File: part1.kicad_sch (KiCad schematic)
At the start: 21 parts, among them U1 74LS377, U10 Am2918, U11 Am2919, U12 Am2919, U13 74LS139, U14 74LS399, U15 74LS175, U16 Am2921, U17 Am2921, U18 Am27S19, U19 Am27S19, U2 Am2919, U3 Am2919, U37 74LS175, U4 Am27S21, U5 Am27S21, U6 Am27S21, U7 Am2910, U8 Am2918, U9 Am2918

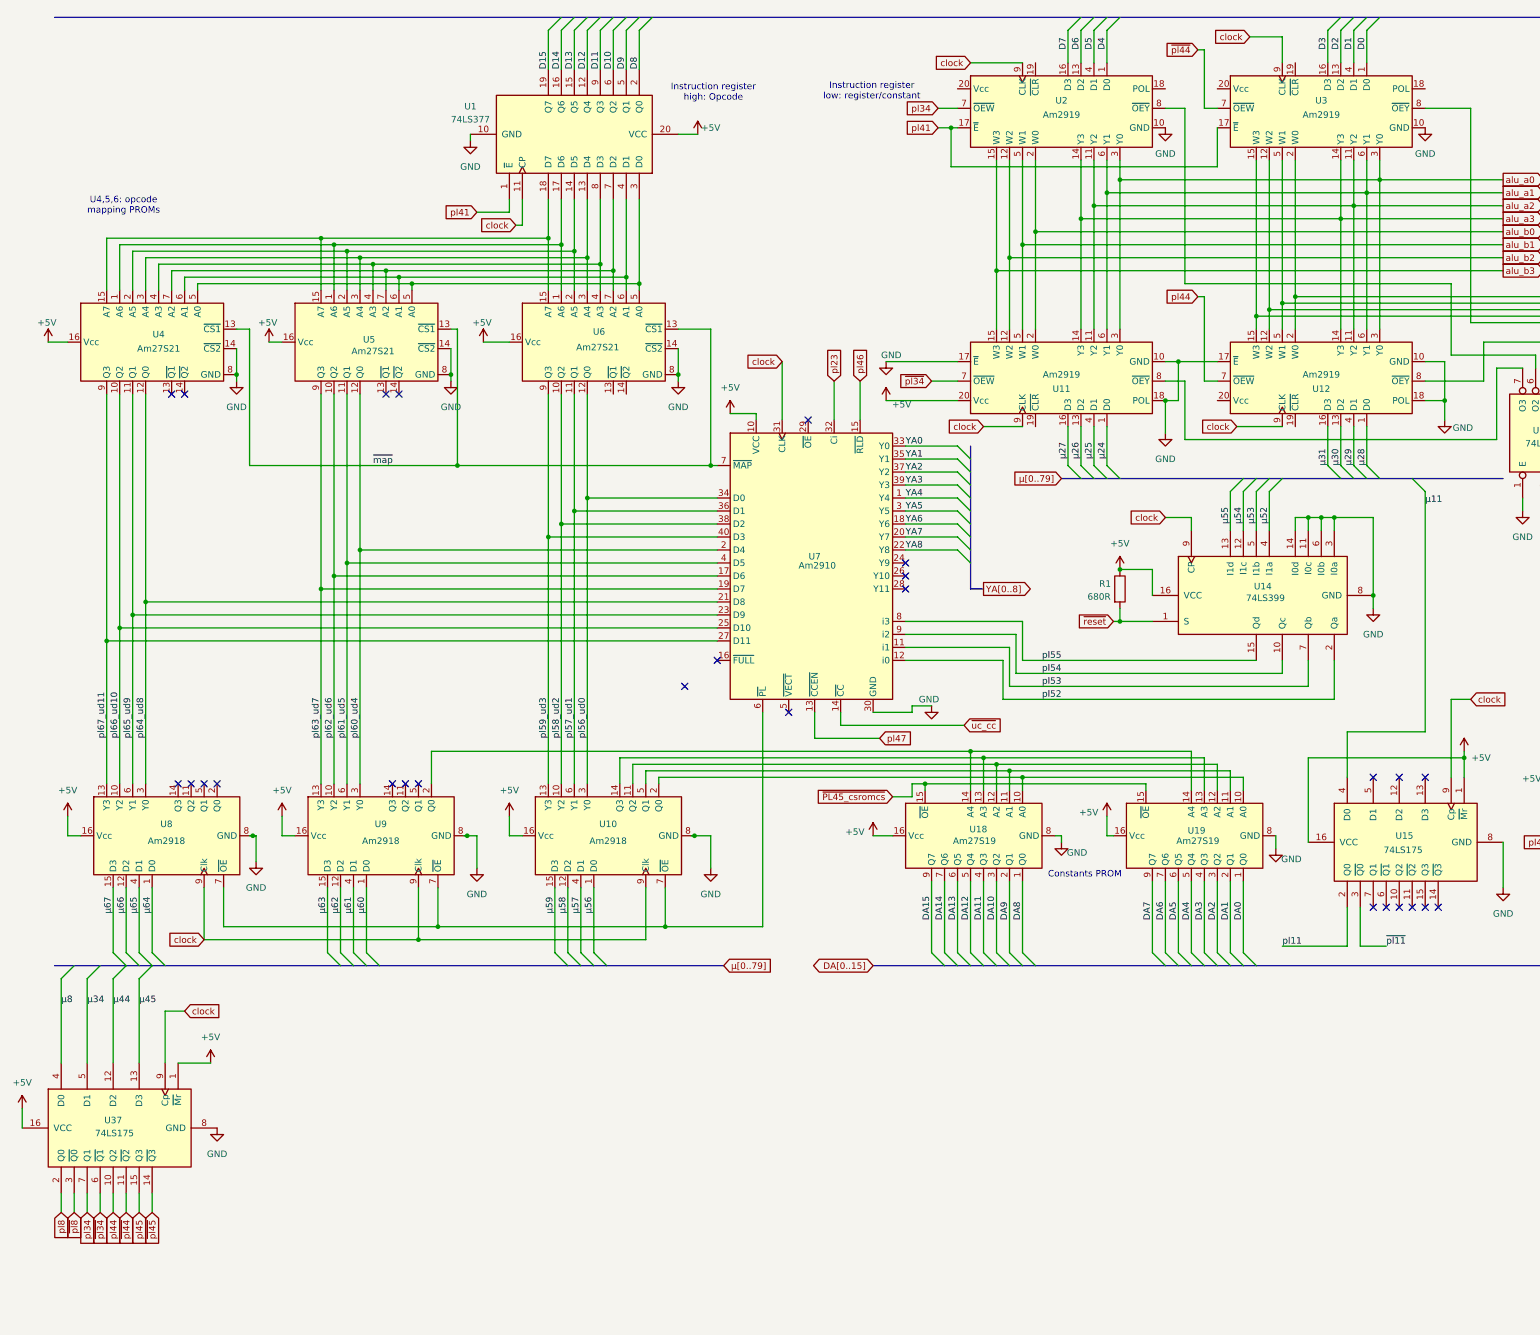
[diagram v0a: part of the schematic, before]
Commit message: Schematic complete wrt original
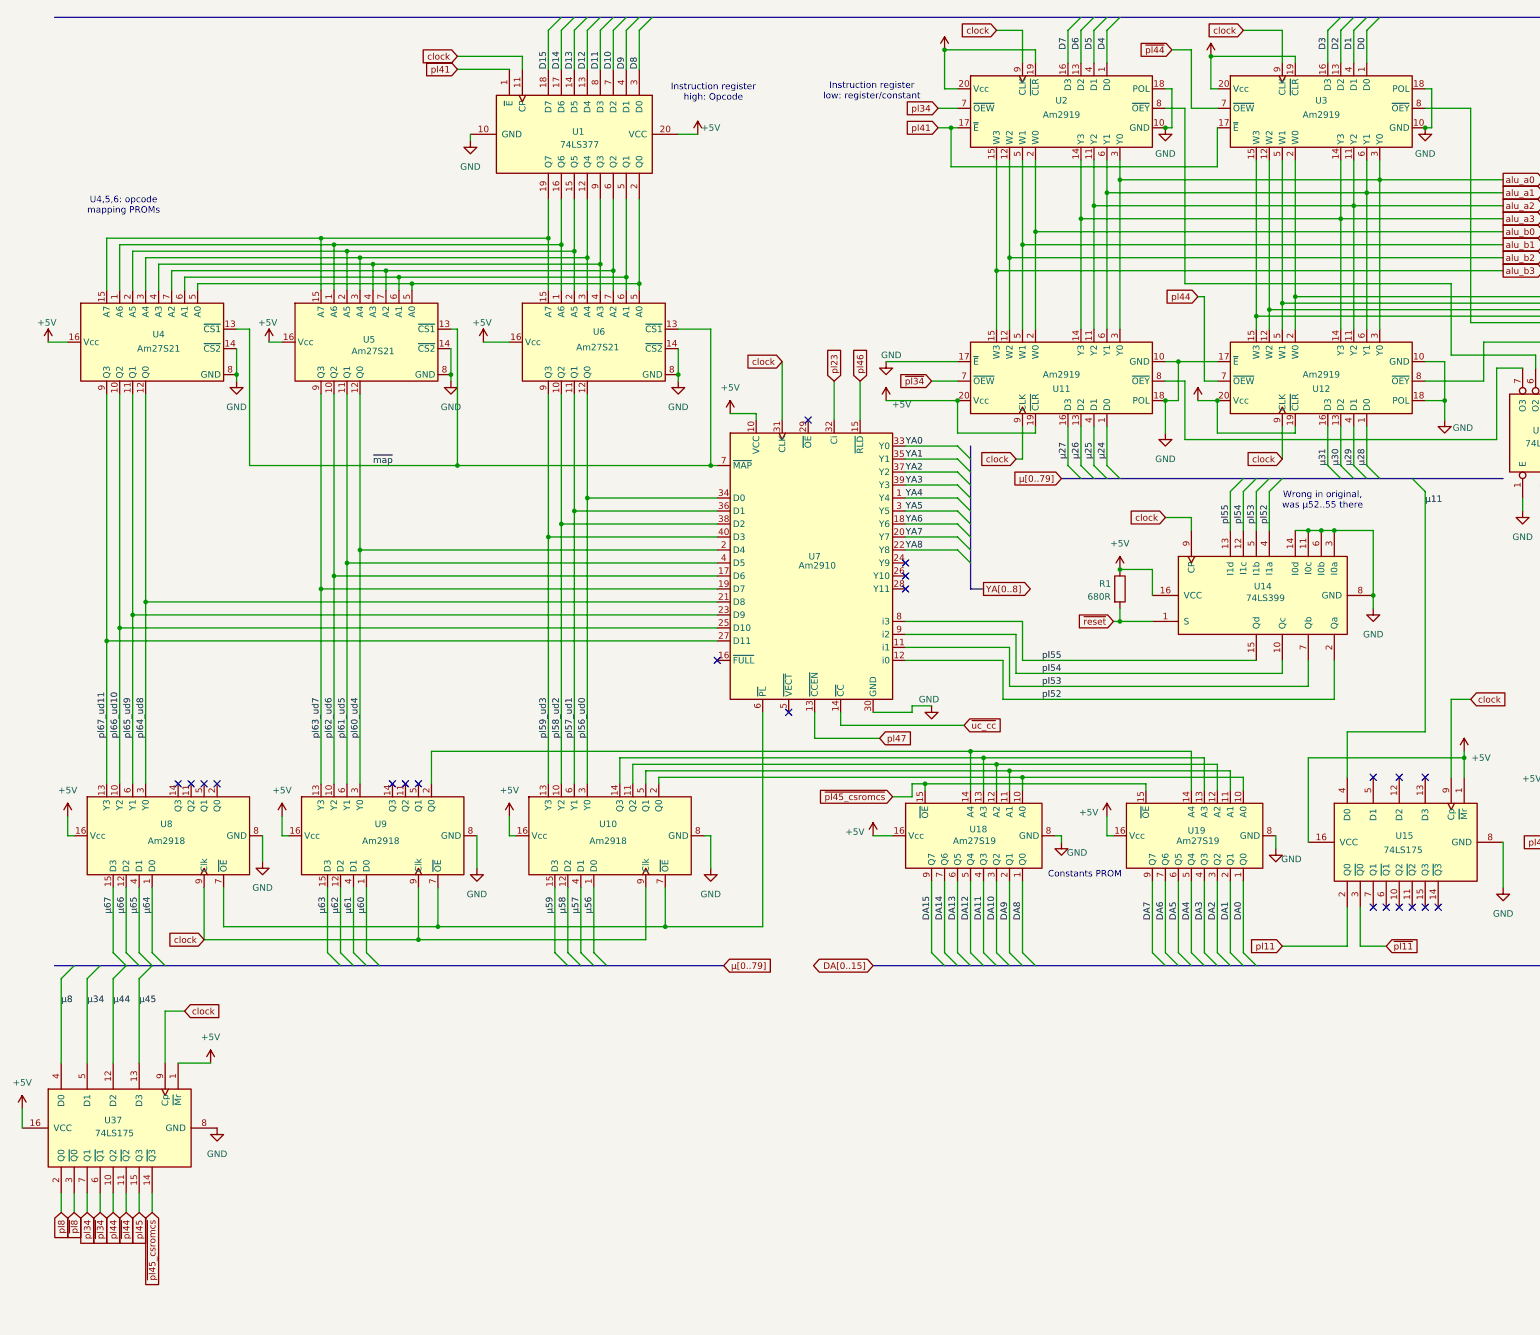
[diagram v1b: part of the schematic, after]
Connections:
- net ~{pl45} is gone; now on net ~{pl45_csromcs}: U37.14 (~{Q3})
- net µ52 is gone; now on net pl52: U14.4 (I1a)
- net µ53 is gone; now on net pl53: U14.5 (I1b)
- net µ54 is gone; now on net pl54: U14.12 (I1c)
- net µ55 is gone; now on net pl55: U14.13 (I1d)
- net +5V: now also U11.19 (~{CLR}), U12.19 (~{CLR}), U12.20 (Vcc), U2.19 (~{CLR}), U2.20 (Vcc), U3.19 (~{CLR}), U3.20 (Vcc)
- net D10: now also U1.7 (D2); no longer U1.6 (Q2)
- net D11: now also U1.8 (D3); no longer U1.9 (Q3)
- net D12: now also U1.13 (D4); no longer U1.12 (Q4)
- net D13: now also U1.14 (D5); no longer U1.15 (Q5)
- net D14: now also U1.17 (D6); no longer U1.16 (Q6)
- net D15: now also U1.18 (D7); no longer U1.19 (Q7)
- net D8: now also U1.3 (D0); no longer U1.2 (Q0)
- net D9: now also U1.4 (D1); no longer U1.5 (Q1)
- net GND: now also U2.18 (POL), U3.18 (POL)
- net at U4.1 (A6), U5.1 (A6), U6.1 (A6): now also U1.16 (Q6); no longer U1.17 (D6)
- net at U4.15 (A7), U5.15 (A7), U6.15 (A7): now also U1.19 (Q7); no longer U1.18 (D7)
- net at U4.2 (A5), U5.2 (A5), U6.2 (A5): now also U1.15 (Q5); no longer U1.14 (D5)
- net at U4.3 (A4), U5.3 (A4), U6.3 (A4): now also U1.12 (Q4); no longer U1.13 (D4)
- net at U4.4 (A3), U5.4 (A3), U6.4 (A3): now also U1.9 (Q3); no longer U1.8 (D3)
- net at U4.5 (A0), U5.5 (A0), U6.5 (A0): now also U1.2 (Q0); no longer U1.3 (D0)
- net at U4.6 (A1), U5.6 (A1), U6.6 (A1): now also U1.5 (Q1); no longer U1.4 (D1)
- net at U4.7 (A2), U5.7 (A2), U6.7 (A2): now also U1.6 (Q2); no longer U1.7 (D2)
- net ~{PL45_csromcs} renamed ~{pl45_csromcs}
- no-connect marks 34 -> 29
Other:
- note added: "Wrong in original, was µ52..55 there"
